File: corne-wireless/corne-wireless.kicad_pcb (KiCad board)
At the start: 2 copper layers, 275.5 x 105.6 mm, 116 parts, among them J2 OLED, J4 OLED, SW1 SW_PUSH, SW10 SW_PUSH, SW11 SW_PUSH, SW12 SW_PUSH, SW13 SW_PUSH, SW14 SW_PUSH, SW15 SW_PUSH, SW16 SW_PUSH, SW17 SW_PUSH, SW18 SW_PUSH, SW19 SW_PUSH, SW2 SW_PUSH, SW20 SW_PUSH, SW21 SW_PUSH, SW22 SW_PUSH, SW23 SW_PUSH, SW24 SW_PUSH, SW25 SW_PUSH, SW26 SW_PUSH, SW27 SW_PUSH, SW28 SW_PUSH, SW29 SW_PUSH, SW3 SW_PUSH, SW30 SW_PUSH, SW31 SW_PUSH, SW32 SW_PUSH, SW33 SW_PUSH, SW34 SW_PUSH, SW35 SW_PUSH, SW36 SW_PUSH, SW37 SW_PUSH, SW38 SW_PUSH, SW39 SW_PUSH, SW4 SW_PUSH, SW40 SW_PUSH, SW41 SW_PUSH, SW42 SW_PUSH, SW5 SW_PUSH, SW6 SW_PUSH, SW7 SW_PUSH, SW8 SW_PUSH, SW9 SW_PUSH, U1 ProMicro, U2 ProMicro

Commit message: Restart
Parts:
- added J1: MJ-4PP-9, kbd:MJ-4PP-9_1side, F.Cu at (144.1, 74.3)
- added J3: MJ-4PP-9, kbd:MJ-4PP-9_1side, F.Cu at (152.5, 74.3)
- added LED1: WS2812B, LED_SMD:LED_WS2812B_PLCC4_5.0x5.0mm_P3.2mm, B.Cu at (39.1, 45.3)
- added LED10: YS-SK6812MINI-E, kbd:YS-SK6812MINI-E, B.Cu at (77.1, 33.4)
- added LED11: YS-SK6812MINI-E, kbd:YS-SK6812MINI-E, B.Cu at (96.1, 35.8)
- added LED12: YS-SK6812MINI-E, kbd:YS-SK6812MINI-E, B.Cu at (115.1, 38.2)
- added LED13: YS-SK6812MINI-E, kbd:YS-SK6812MINI-E, B.Cu at (20.1, 59.5)
- added LED14: YS-SK6812MINI-E, kbd:YS-SK6812MINI-E, B.Cu at (39.1, 59.5)
- added LED15: YS-SK6812MINI-E, kbd:YS-SK6812MINI-E, B.Cu at (58.1, 54.8)
- added LED16: YS-SK6812MINI-E, kbd:YS-SK6812MINI-E, B.Cu at (77.1, 52.4)
- added LED17: YS-SK6812MINI-E, kbd:YS-SK6812MINI-E, B.Cu at (96.1, 54.8)
- added LED18: YS-SK6812MINI-E, kbd:YS-SK6812MINI-E, B.Cu at (115.1, 57.2)
- added LED19: YS-SK6812MINI-E, kbd:YS-SK6812MINI-E, B.Cu at (20.1, 78.5)
- added LED2: WS2812B, LED_SMD:LED_WS2812B_PLCC4_5.0x5.0mm_P3.2mm, B.Cu at (77.1, 38.2)
- added LED20: YS-SK6812MINI-E, kbd:YS-SK6812MINI-E, B.Cu at (39.1, 78.5)
- added LED21: YS-SK6812MINI-E, kbd:YS-SK6812MINI-E, B.Cu at (58.1, 73.8)
- added LED22: YS-SK6812MINI-E, kbd:YS-SK6812MINI-E, B.Cu at (77.1, 71.4)
- added LED23: YS-SK6812MINI-E, kbd:YS-SK6812MINI-E, B.Cu at (96.1, 73.8)
- added LED24: YS-SK6812MINI-E, kbd:YS-SK6812MINI-E, B.Cu at (115.1, 76.2)
- added LED25: YS-SK6812MINI-E, kbd:YS-SK6812MINI-E, B.Cu at (86.6, 93.4)
- added LED26: YS-SK6812MINI-E, kbd:YS-SK6812MINI-E, B.Cu at (106.4, 96.0)
- added LED27: YS-SK6812MINI-E, kbd:YS-SK6812MINI-E, B.Cu at (134.0, 97.5)
- added LED28: WS2812B, LED_SMD:LED_WS2812B_PLCC4_5.0x5.0mm_P3.2mm, B.Cu at (257.6, 45.3)
- added LED29: WS2812B, LED_SMD:LED_WS2812B_PLCC4_5.0x5.0mm_P3.2mm, B.Cu at (219.6, 38.2)
- added LED3: WS2812B, LED_SMD:LED_WS2812B_PLCC4_5.0x5.0mm_P3.2mm, B.Cu at (115.1, 42.9)
- added LED30: WS2812B, LED_SMD:LED_WS2812B_PLCC4_5.0x5.0mm_P3.2mm, B.Cu at (181.6, 42.9)
- added LED31: WS2812B, LED_SMD:LED_WS2812B_PLCC4_5.0x5.0mm_P3.2mm, B.Cu at (257.6, 64.3)
- added LED32: WS2812B, LED_SMD:LED_WS2812B_PLCC4_5.0x5.0mm_P3.2mm, B.Cu at (219.6, 76.2)
- added LED33: WS2812B, LED_SMD:LED_WS2812B_PLCC4_5.0x5.0mm_P3.2mm, B.Cu at (181.6, 80.9)
- added LED34: YS-SK6812MINI-E, kbd:YS-SK6812MINI-E, B.Cu at (276.6, 40.5)
- added LED35: YS-SK6812MINI-E, kbd:YS-SK6812MINI-E, B.Cu at (257.6, 40.5)
- added LED36: YS-SK6812MINI-E, kbd:YS-SK6812MINI-E, B.Cu at (238.6, 35.8)
- added LED37: YS-SK6812MINI-E, kbd:YS-SK6812MINI-E, B.Cu at (219.6, 33.4)
- added LED38: YS-SK6812MINI-E, kbd:YS-SK6812MINI-E, B.Cu at (200.6, 35.8)
- added LED39: YS-SK6812MINI-E, kbd:YS-SK6812MINI-E, B.Cu at (181.6, 38.2)
- added LED4: WS2812B, LED_SMD:LED_WS2812B_PLCC4_5.0x5.0mm_P3.2mm, B.Cu at (39.1, 64.3)
- added LED40: YS-SK6812MINI-E, kbd:YS-SK6812MINI-E, B.Cu at (276.6, 59.5)
- added LED41: YS-SK6812MINI-E, kbd:YS-SK6812MINI-E, B.Cu at (257.6, 59.5)
- added LED42: YS-SK6812MINI-E, kbd:YS-SK6812MINI-E, B.Cu at (238.6, 54.8)
- added LED43: YS-SK6812MINI-E, kbd:YS-SK6812MINI-E, B.Cu at (219.6, 52.4)
- added LED44: YS-SK6812MINI-E, kbd:YS-SK6812MINI-E, B.Cu at (200.6, 54.8)
- added LED45: YS-SK6812MINI-E, kbd:YS-SK6812MINI-E, B.Cu at (181.6, 57.2)
- added LED46: YS-SK6812MINI-E, kbd:YS-SK6812MINI-E, B.Cu at (276.6, 78.5)
- added LED47: YS-SK6812MINI-E, kbd:YS-SK6812MINI-E, B.Cu at (257.6, 78.5)
- added LED48: YS-SK6812MINI-E, kbd:YS-SK6812MINI-E, B.Cu at (238.6, 73.8)
- added LED49: YS-SK6812MINI-E, kbd:YS-SK6812MINI-E, B.Cu at (219.6, 71.4)
- added LED5: WS2812B, LED_SMD:LED_WS2812B_PLCC4_5.0x5.0mm_P3.2mm, B.Cu at (77.1, 76.2)
- added LED50: YS-SK6812MINI-E, kbd:YS-SK6812MINI-E, B.Cu at (200.6, 73.8)
- added LED51: YS-SK6812MINI-E, kbd:YS-SK6812MINI-E, B.Cu at (181.6, 76.2)
- added LED52: YS-SK6812MINI-E, kbd:YS-SK6812MINI-E, B.Cu at (210.1, 93.4)
- added LED53: YS-SK6812MINI-E, kbd:YS-SK6812MINI-E, B.Cu at (190.3, 96.0)
- added LED54: YS-SK6812MINI-E, kbd:YS-SK6812MINI-E, B.Cu at (162.8, 97.5)
- added LED6: WS2812B, LED_SMD:LED_WS2812B_PLCC4_5.0x5.0mm_P3.2mm, B.Cu at (115.1, 80.9)
- added LED7: YS-SK6812MINI-E, kbd:YS-SK6812MINI-E, B.Cu at (20.1, 40.5)
- added LED8: YS-SK6812MINI-E, kbd:YS-SK6812MINI-E, B.Cu at (39.1, 40.5)
- added LED9: YS-SK6812MINI-E, kbd:YS-SK6812MINI-E, B.Cu at (58.1, 35.8)
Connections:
- D1 pad 1: row0 -> unconnected-(D1-K-Pad1)
- D1 pad 2: Net-(D1-Pad2) -> Net-(D1-A)
- D10 pad 1: row1 -> unconnected-(D10-K-Pad1)
- D10 pad 2: Net-(D10-Pad2) -> Net-(D10-A)
- D11 pad 1: row1 -> unconnected-(D11-K-Pad1)
- D11 pad 2: Net-(D11-Pad2) -> Net-(D11-A)
- D12 pad 2: Net-(D12-Pad2) -> Net-(D12-A)
- D13 pad 1: row2 -> unconnected-(D13-K-Pad1)
- D13 pad 2: Net-(D13-Pad2) -> Net-(D13-A)
- D14 pad 1: row2 -> unconnected-(D14-K-Pad1)
- D14 pad 2: Net-(D14-Pad2) -> Net-(D14-A)
- D15 pad 1: row2 -> unconnected-(D15-K-Pad1)
- D15 pad 2: Net-(D15-Pad2) -> Net-(D15-A)
- D16 pad 1: row2 -> unconnected-(D16-K-Pad1)
- D16 pad 2: Net-(D16-Pad2) -> Net-(D16-A)
- D17 pad 1: row2 -> unconnected-(D17-K-Pad1)
- D17 pad 2: Net-(D17-Pad2) -> Net-(D17-A)
- D18 pad 2: Net-(D18-Pad2) -> Net-(D18-A)
- D19 pad 1: row3 -> unconnected-(D19-K-Pad1)
- D19 pad 2: Net-(D19-Pad2) -> Net-(D19-A)
- D2 pad 1: row0 -> unconnected-(D2-K-Pad1)
- D2 pad 2: Net-(D2-Pad2) -> Net-(D2-A)
- D20 pad 1: row3 -> unconnected-(D20-K-Pad1)
- D20 pad 2: Net-(D20-Pad2) -> Net-(D20-A)
- D21 pad 2: Net-(D21-Pad2) -> Net-(D21-A)
- D22 pad 1: row0_r -> unconnected-(D22-K-Pad1)
- D22 pad 2: Net-(D22-Pad2) -> Net-(D22-A)
- D23 pad 1: row0_r -> unconnected-(D23-K-Pad1)
- D23 pad 2: Net-(D23-Pad2) -> Net-(D23-A)
- D24 pad 1: row0_r -> unconnected-(D24-K-Pad1)
- D24 pad 2: Net-(D24-Pad2) -> Net-(D24-A)
- D25 pad 1: row0_r -> unconnected-(D25-K-Pad1)
- D25 pad 2: Net-(D25-Pad2) -> Net-(D25-A)
- D26 pad 1: row0_r -> unconnected-(D26-K-Pad1)
- D26 pad 2: Net-(D26-Pad2) -> Net-(D26-A)
- D27 pad 2: Net-(D27-Pad2) -> Net-(D27-A)
- D28 pad 1: row1_r -> unconnected-(D28-K-Pad1)
- D28 pad 2: Net-(D28-Pad2) -> Net-(D28-A)
- D29 pad 1: row1_r -> unconnected-(D29-K-Pad1)
- D29 pad 2: Net-(D29-Pad2) -> Net-(D29-A)
- D3 pad 1: row0 -> unconnected-(D3-K-Pad1)
- D3 pad 2: Net-(D3-Pad2) -> Net-(D3-A)
- D30 pad 1: row1_r -> unconnected-(D30-K-Pad1)
- D30 pad 2: Net-(D30-Pad2) -> Net-(D30-A)
- D31 pad 1: row1_r -> unconnected-(D31-K-Pad1)
- D31 pad 2: Net-(D31-Pad2) -> Net-(D31-A)
- D32 pad 1: row1_r -> unconnected-(D32-K-Pad1)
- D32 pad 2: Net-(D32-Pad2) -> Net-(D32-A)
- D33 pad 2: Net-(D33-Pad2) -> Net-(D33-A)
- D34 pad 1: row2_r -> unconnected-(D34-K-Pad1)
- D34 pad 2: Net-(D34-Pad2) -> Net-(D34-A)
- D35 pad 1: row2_r -> unconnected-(D35-K-Pad1)
- D35 pad 2: Net-(D35-Pad2) -> Net-(D35-A)
- D36 pad 1: row2_r -> unconnected-(D36-K-Pad1)
- D36 pad 2: Net-(D36-Pad2) -> Net-(D36-A)
- D37 pad 1: row2_r -> unconnected-(D37-K-Pad1)
- D37 pad 2: Net-(D37-Pad2) -> Net-(D37-A)
- D38 pad 1: row2_r -> unconnected-(D38-K-Pad1)
- D38 pad 2: Net-(D38-Pad2) -> Net-(D38-A)
- D39 pad 2: Net-(D39-Pad2) -> Net-(D39-A)
- D4 pad 1: row0 -> unconnected-(D4-K-Pad1)
- D4 pad 2: Net-(D4-Pad2) -> Net-(D4-A)
- D40 pad 1: row3_r -> unconnected-(D40-K-Pad1)
- D40 pad 2: Net-(D40-Pad2) -> Net-(D40-A)
- D41 pad 1: row3_r -> unconnected-(D41-K-Pad1)
- D41 pad 2: Net-(D41-Pad2) -> Net-(D41-A)
- D42 pad 2: Net-(D42-Pad2) -> Net-(D42-A)
- D5 pad 1: row0 -> unconnected-(D5-K-Pad1)
- D5 pad 2: Net-(D5-Pad2) -> Net-(D5-A)
- D6 pad 2: Net-(D6-Pad2) -> Net-(D6-A)
- D7 pad 1: row1 -> unconnected-(D7-K-Pad1)
- D7 pad 2: Net-(D7-Pad2) -> Net-(D7-A)
- D8 pad 1: row1 -> unconnected-(D8-K-Pad1)
- D8 pad 2: Net-(D8-Pad2) -> Net-(D8-A)
- D9 pad 1: row1 -> unconnected-(D9-K-Pad1)
- D9 pad 2: Net-(D9-Pad2) -> Net-(D9-A)
- SW1 pad 2: unconnected-(SW1-Pad2) -> Net-(D1-A)
- SW10 pad 2: unconnected-(SW10-Pad2) -> Net-(D10-A)
- SW11 pad 2: unconnected-(SW11-Pad2) -> Net-(D11-A)
- SW12 pad 2: unconnected-(SW12-Pad2) -> Net-(D12-A)
- SW13 pad 2: unconnected-(SW13-Pad2) -> Net-(D13-A)
- SW14 pad 2: unconnected-(SW14-Pad2) -> Net-(D14-A)
- SW15 pad 2: unconnected-(SW15-Pad2) -> Net-(D15-A)
- SW16 pad 2: unconnected-(SW16-Pad2) -> Net-(D16-A)
- SW17 pad 2: unconnected-(SW17-Pad2) -> Net-(D17-A)
- SW18 pad 2: unconnected-(SW18-Pad2) -> Net-(D18-A)
- SW19 pad 2: unconnected-(SW19-Pad2) -> Net-(D19-A)
- SW2 pad 2: unconnected-(SW2-Pad2) -> Net-(D2-A)
- SW20 pad 2: unconnected-(SW20-Pad2) -> Net-(D20-A)
- SW21 pad 2: unconnected-(SW21-Pad2) -> Net-(D21-A)
- SW22 pad 2: unconnected-(SW22-Pad2) -> Net-(D22-A)
- SW23 pad 2: unconnected-(SW23-Pad2) -> Net-(D23-A)
- SW24 pad 2: unconnected-(SW24-Pad2) -> Net-(D24-A)
- SW25 pad 2: unconnected-(SW25-Pad2) -> Net-(D25-A)
- SW26 pad 2: unconnected-(SW26-Pad2) -> Net-(D26-A)
- SW27 pad 2: unconnected-(SW27-Pad2) -> Net-(D27-A)
- SW28 pad 2: unconnected-(SW28-Pad2) -> Net-(D28-A)
- SW29 pad 2: unconnected-(SW29-Pad2) -> Net-(D29-A)
- SW3 pad 2: unconnected-(SW3-Pad2) -> Net-(D3-A)
- SW30 pad 2: unconnected-(SW30-Pad2) -> Net-(D30-A)
- SW31 pad 2: unconnected-(SW31-Pad2) -> Net-(D31-A)
- SW32 pad 2: unconnected-(SW32-Pad2) -> Net-(D32-A)
- SW33 pad 2: unconnected-(SW33-Pad2) -> Net-(D33-A)
- SW34 pad 2: unconnected-(SW34-Pad2) -> Net-(D34-A)
- SW35 pad 2: unconnected-(SW35-Pad2) -> Net-(D35-A)
- SW36 pad 2: unconnected-(SW36-Pad2) -> Net-(D36-A)
- SW37 pad 2: unconnected-(SW37-Pad2) -> Net-(D37-A)
- SW38 pad 2: unconnected-(SW38-Pad2) -> Net-(D38-A)
- SW39 pad 2: unconnected-(SW39-Pad2) -> Net-(D39-A)
- SW4 pad 2: unconnected-(SW4-Pad2) -> Net-(D4-A)
- SW40 pad 2: unconnected-(SW40-Pad2) -> Net-(D40-A)
- SW41 pad 2: unconnected-(SW41-Pad2) -> Net-(D41-A)
- SW42 pad 2: unconnected-(SW42-Pad2) -> Net-(D42-A)
- SW5 pad 2: unconnected-(SW5-Pad2) -> Net-(D5-A)
- SW6 pad 2: unconnected-(SW6-Pad2) -> Net-(D6-A)
- SW7 pad 2: unconnected-(SW7-Pad2) -> Net-(D7-A)
- SW8 pad 2: unconnected-(SW8-Pad2) -> Net-(D8-A)
- SW9 pad 2: unconnected-(SW9-Pad2) -> Net-(D9-A)
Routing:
- net GND: track 49.9 -> 637.2 mm, vias 0 -> 16
- net GNDA: track 49.6 -> 617.9 mm, vias 0 -> 15
- net VDD: track 37.6 -> 573.1 mm, vias 0 -> 2
- net VCC: track 37.3 -> 544.3 mm, vias 0 -> 2
- net data: track 0.00 -> 77.0 mm
- net Net-(LED31-Pad2): track 0.00 -> 71.8 mm, vias 0 -> 2
- net data_r: track 0.00 -> 62.9 mm
- net Net-(LED1-Pad4): track 0.00 -> 47.8 mm
- net Net-(LED32-Pad2): track 0.00 -> 47.4 mm
- net Net-(LED2-Pad4): track 0.00 -> 46.3 mm
- net Net-(LED4-Pad2): track 0.00 -> 43.6 mm, vias 0 -> 2
- net Net-(LED28-Pad2): track 0.00 -> 41.5 mm, vias 0 -> 2
- net LED: track 0.00 -> 41.1 mm
- net Net-(D21-Pad2): track 38.3 -> 0.00 mm
- net Net-(D21-A): track 0.00 -> 38.3 mm
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
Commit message: Prep for removal of OLED headers
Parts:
- removed J1, J3: MJ-4PP-9, kbd:MJ-4PP-9_1side
- removed J2, J4: OLED, kbd:OLED_1side
- removed LED1, LED2, LED28, LED29, LED3, LED30, LED31, LED32, LED33, LED4, LED5, LED6: WS2812B, LED_SMD:LED_WS2812B_PLCC4_5.0x5.0mm_P3.2mm
- removed LED10, LED11, LED12, LED13, LED14, LED15, LED16, LED17, LED18, LED19, LED20, LED21, LED22, LED23, LED24, LED25, LED26, LED27, LED34, LED35, LED36, LED37, LED38, LED39, LED40, LED41, LED42, LED43, LED44, LED45, LED46, LED47, LED48, LED49, LED50, LED51, LED52, LED53, LED54, LED7, LED8, LED9: YS-SK6812MINI-E, kbd:YS-SK6812MINI-E
- added OL1: OLED, kbd:OLED_1side, F.Cu at (130.9, 67.2)
- added OL2: OLED, kbd:OLED_1side, F.Cu at (158.3, 67.2)
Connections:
- D1 pad 1: unconnected-(D1-K-Pad1) -> row0
- D10 pad 1: unconnected-(D10-K-Pad1) -> row1
- D11 pad 1: unconnected-(D11-K-Pad1) -> row1
- D13 pad 1: unconnected-(D13-K-Pad1) -> row2
- D14 pad 1: unconnected-(D14-K-Pad1) -> row2
- D15 pad 1: unconnected-(D15-K-Pad1) -> row2
- D16 pad 1: unconnected-(D16-K-Pad1) -> row2
- D17 pad 1: unconnected-(D17-K-Pad1) -> row2
- D19 pad 1: unconnected-(D19-K-Pad1) -> row3
- D2 pad 1: unconnected-(D2-K-Pad1) -> row0
- D20 pad 1: unconnected-(D20-K-Pad1) -> row3
- D22 pad 1: unconnected-(D22-K-Pad1) -> row0_r
- D23 pad 1: unconnected-(D23-K-Pad1) -> row0_r
- D24 pad 1: unconnected-(D24-K-Pad1) -> row0_r
- D25 pad 1: unconnected-(D25-K-Pad1) -> row0_r
- D26 pad 1: unconnected-(D26-K-Pad1) -> row0_r
- D28 pad 1: unconnected-(D28-K-Pad1) -> row1_r
- D29 pad 1: unconnected-(D29-K-Pad1) -> row1_r
- D3 pad 1: unconnected-(D3-K-Pad1) -> row0
- D30 pad 1: unconnected-(D30-K-Pad1) -> row1_r
- D31 pad 1: unconnected-(D31-K-Pad1) -> row1_r
- D32 pad 1: unconnected-(D32-K-Pad1) -> row1_r
- D34 pad 1: unconnected-(D34-K-Pad1) -> row2_r
- D35 pad 1: unconnected-(D35-K-Pad1) -> row2_r
- D36 pad 1: unconnected-(D36-K-Pad1) -> row2_r
- D37 pad 1: unconnected-(D37-K-Pad1) -> row2_r
- D38 pad 1: unconnected-(D38-K-Pad1) -> row2_r
- D4 pad 1: unconnected-(D4-K-Pad1) -> row0
- D40 pad 1: unconnected-(D40-K-Pad1) -> row3_r
- D41 pad 1: unconnected-(D41-K-Pad1) -> row3_r
- D5 pad 1: unconnected-(D5-K-Pad1) -> row0
- D7 pad 1: unconnected-(D7-K-Pad1) -> row1
- D8 pad 1: unconnected-(D8-K-Pad1) -> row1
- D9 pad 1: unconnected-(D9-K-Pad1) -> row1
- RSW1 pad 2: unconnected-(RSW1-Pad2) -> GND1
- RSW2 pad 2: unconnected-(RSW2-Pad2) -> GND2
- U1 pad 21: unconnected-(U1-VCC-Pad21) -> VCC
- U1 pad 23: unconnected-(U1-GND-Pad23) -> GND1
- U1 pad 3: Net-(U1-GND-Pad3) -> GND1
- U1 pad 4: Net-(U1-GND-Pad3) -> GND1
- U2 pad 21: unconnected-(U2-VCC-Pad21) -> VDD
- U2 pad 23: unconnected-(U2-GND-Pad23) -> GND2
- U2 pad 3: Net-(U2-GND-Pad3) -> GND2
- U2 pad 4: Net-(U2-GND-Pad3) -> GND2
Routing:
- net GND: track 637.2 -> 0.00 mm, vias 16 -> 0
- net GNDA: track 617.9 -> 0.00 mm, vias 15 -> 0
- net VDD: track 573.1 -> 37.6 mm, vias 2 -> 0
- net VCC: track 544.3 -> 37.3 mm, vias 2 -> 0
- net GND2: track 0.00 -> 78.1 mm
- net data: track 77.0 -> 0.00 mm
- net Net-(LED31-Pad2): track 71.8 -> 0.00 mm, vias 2 -> 0
- net data_r: track 62.9 -> 0.00 mm
- net GND1: track 0.00 -> 49.9 mm
- net Net-(LED1-Pad4): track 47.8 -> 0.00 mm
- net Net-(LED32-Pad2): track 47.4 -> 0.00 mm
- net Net-(LED2-Pad4): track 46.3 -> 0.00 mm
- net Net-(LED4-Pad2): track 43.6 -> 0.00 mm, vias 2 -> 0
- net Net-(LED28-Pad2): track 41.5 -> 0.00 mm, vias 2 -> 0
- net LED: track 41.1 -> 0.00 mm
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
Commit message: Finalize PCB
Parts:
- removed OL1, OL2: OLED, kbd:OLED_1side
- added J1: Conn_01x02, Connector_JST:JST_SH_BM02B-SRSS-TB_1x02-1MP_P1.00mm_Vertical, F.Cu at (129.7, 67.4)
- added J2: Conn_01x02, Connector_JST:JST_SH_BM02B-SRSS-TB_1x02-1MP_P1.00mm_Vertical, F.Cu at (167.2, 67.4)
- added PMOS1: SSM3J328R, corne-wireless-fp:SOT-23F, F.Cu at (133.6, 74.2)
- added PMOS2: SSM3J328R, corne-wireless-fp:SOT-23F, F.Cu at (163.6, 74.2)
- added SW1: SW_SPDT, Button_Switch_SMD:SW_SPDT_PCM12, F.Cu at (142.8, 76.3)
- added SW23: SW_SPDT, Button_Switch_SMD:SW_SPDT_PCM12, F.Cu at (154.4, 76.3)
- renumbered D4 to D10, D10 to D11, D16 to D12, D19 to D13, D5 to D14, D11 to D15, D17 to D16, D20 to D17, D6 to D18, D12 to D19, D7 to D2, D18 to D20, D28 to D23, D34 to D24, D23 to D25, D29 to D26, D35 to D27, D24 to D28, D30 to D29, D13 to D3, D36 to D30, D25 to D31, D31 to D32, D37 to D33, D40 to D34, D26 to D35, D32 to D36, D38 to D37, D41 to D38, D27 to D39, D2 to D4, D33 to D40, D39 to D41, D8 to D5, D14 to D6, D3 to D7, D9 to D8, D15 to D9, SW15 to SW10, SW4 to SW11, SW10 to SW12, SW16 to SW13, SW19 to SW14, SW5 to SW15, SW11 to SW16, SW20 to SW18, SW6 to SW19, SW1 to SW2, SW12 to SW20, SW18 to SW21, SW21 to SW22, SW22 to SW24, SW28 to SW25, SW34 to SW26, SW23 to SW27, SW29 to SW28, SW35 to SW29, SW7 to SW3, SW24 to SW30, SW30 to SW31, SW36 to SW32, SW25 to SW33, SW31 to SW34, SW37 to SW35, SW40 to SW36, SW26 to SW37, SW32 to SW38, SW38 to SW39, SW13 to SW4, SW41 to SW40, SW27 to SW41, SW33 to SW42, SW39 to SW43, SW42 to SW44, SW2 to SW5, SW8 to SW6, SW14 to SW7, SW3 to SW8
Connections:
- U1 pad 1: LED -> unconnected-(U1-TX0/D3-Pad1)
- U1 pad 2: data -> unconnected-(U1-RX1/D2-Pad2)
- U1 pad 24: unconnected-(U1-RAW-Pad24) -> battery+
- U2 pad 1: LED_r -> unconnected-(U2-TX0/D3-Pad1)
- U2 pad 2: data_r -> unconnected-(U2-RX1/D2-Pad2)
- U2 pad 24: unconnected-(U2-RAW-Pad24) -> battery+_r
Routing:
- net battery+: track 0.00 -> 53.7 mm
- net battery+_r: track 0.00 -> 49.9 mm
- net reset_r: track 85.4 -> 40.0 mm
- net VDD: track 37.6 -> 0.00 mm
- net VCC: track 37.3 -> 0.00 mm
- net SDA_r: track 32.7 -> 0.00 mm
- net SDA: track 32.4 -> 0.00 mm
- net SCL_r: track 27.9 -> 0.00 mm
- net SCL: track 27.7 -> 0.00 mm
- net GND1: track 49.9 -> 70.1 mm, vias 0 -> 3
- net reset: track 60.0 -> 45.8 mm, vias 0 -> 2
- net Net-(J1-Pin_1): track 0.00 -> 7.87 mm
- net Net-(PMOS1-S): track 0.00 -> 7.39 mm
- net Net-(PMOS2-S): track 0.00 -> 7.19 mm
- net Net-(J2-Pin_1): track 0.00 -> 6.89 mm
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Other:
- rule pad_to_mask_clearance: 0.2 -> 0

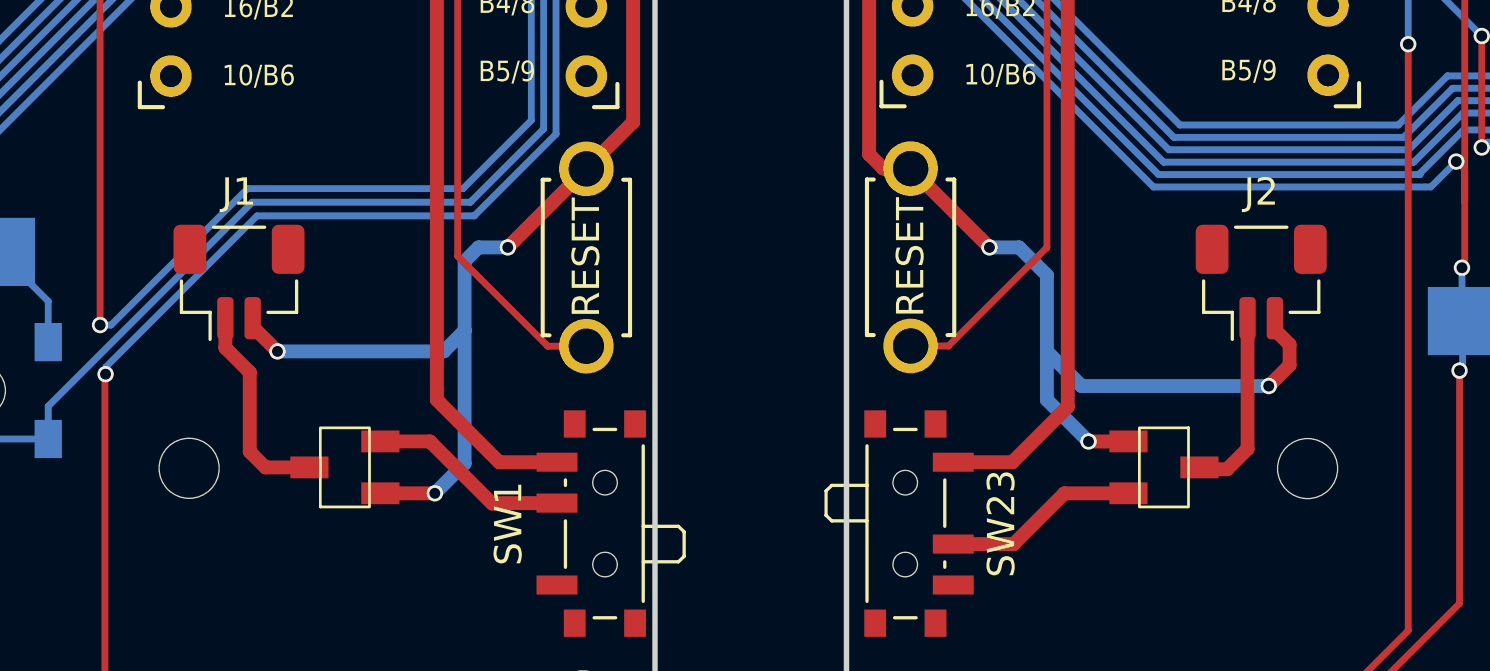
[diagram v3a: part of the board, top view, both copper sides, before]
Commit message: Change JST SH connector to PH
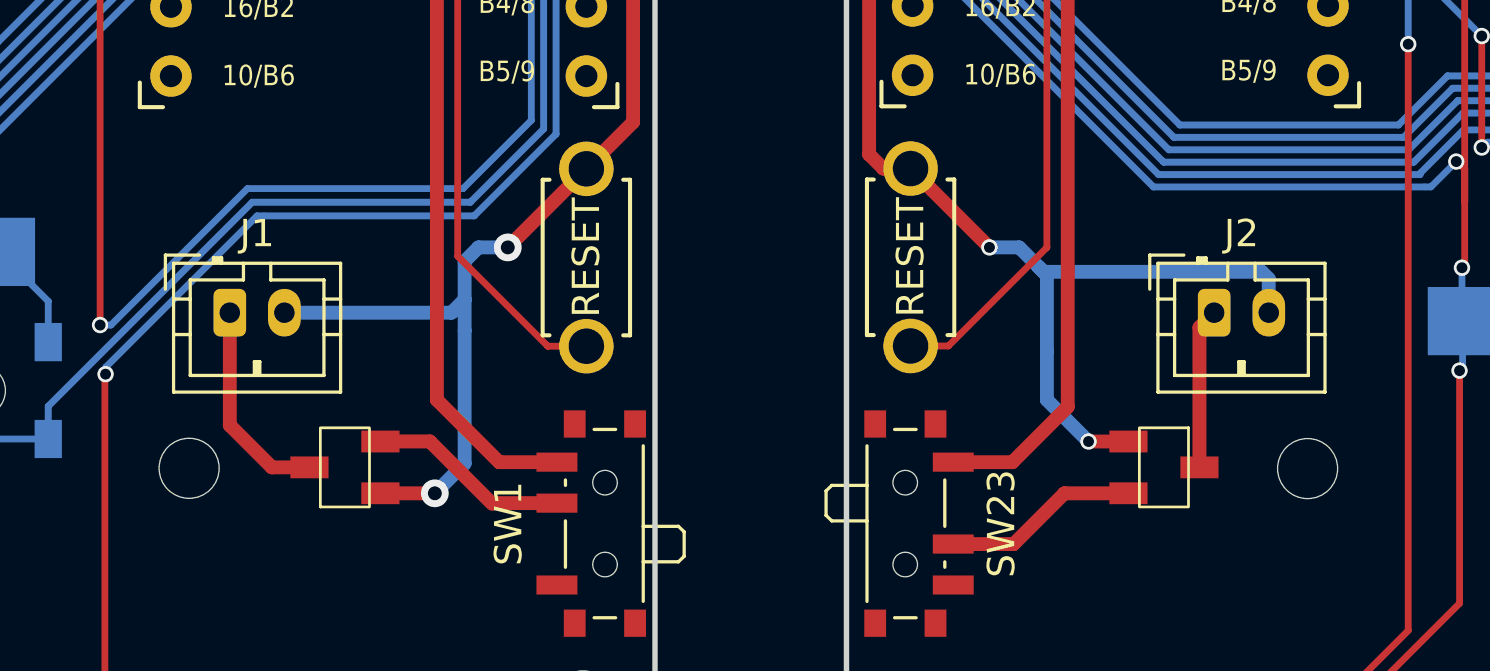
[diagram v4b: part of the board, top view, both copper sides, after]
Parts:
- J1, J2: footprint Connector_JST:JST_SH_BM02B-SRSS-TB_1x02-1MP_P1.00mm_Vertical -> Connector_JST:JST_PH_B2B-PH-K_1x02_P2.00mm_Vertical
- moved J2 2.06 mm to (165.4, 68.6)
- moved J1 1.17 mm to (129.4, 68.6)
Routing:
- net GND1: track 70.1 -> 67.6 mm, vias 3 -> 2
- net GND2: track 76.1 -> 74.3 mm, vias 3 -> 2
- net Net-(J2-Pin_1): track 6.89 -> 5.94 mm

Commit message: Finalize PCB
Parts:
- moved SW23 0.24 mm to (154.2, 76.3)
- moved SW1 0.15 mm to (142.6, 76.3)
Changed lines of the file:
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@@
     (tags "mounting hole 2.2mm no annular m2")
     (attr exclude_from_pos_files exclude_from_bom)
-    (fp_text reference "Ref**" (at -0.95 -0.55) (layer "F.Fab") hide
+    (fp_text reference "Ref**" (at 0.188 2.708) (layer "F.Fab") hide
         (effects (font (size 1 1) (thickness 0.15)))
     )
-    (fp_text value "Val**" (at 0 0.55) (layer "F.Fab") hide
+    (fp_text value "Val**" (at -0.066 0.93) (layer "F.Fab") hide
         (effects (font (size 1 1) (thickness 0.15)))
     )
@@
         (effects (font (size 1 1) (thickness 0.15)))
     )
-    (fp_text value "Conn_01x02" (at 1 4) (layer "F.Fab") hide
+    (fp_text value "Conn_01x02" (at 0.73 4.092) (layer "F.Fab") hide
         (effects (font (size 1 1) (thickness 0.15)))
     )
@@
   )
   (footprint "Button_Switch_SMD:SW_SPDT_PCM12" (layer "F.Cu")
-    (at 142.7775 76.28 90)
+    (at 142.6295 76.28 90)
     (descr "Ultraminiature Surface Mount Slide Switch, right-angle, https://www.ckswitches.com/media/1424/pcm.pdf")
     (property "Sheetfile" "corne-wireless.kicad_sch")
@@
   )
   (footprint "Button_Switch_SMD:SW_SPDT_PCM12" (layer "F.Cu")
-    (at 154.4375 76.28 -90)
+    (at 154.2015 76.28 -90)
     (descr "Ultraminiature Surface Mount Slide Switch, right-angle, https://www.ckswitches.com/media/1424/pcm.pdf")
     (property "Sheetfile" "corne-wireless.kicad_sch")
@@
   (segment (start 153.621901 35.214999) (end 153.414501 35.214999) (width 0.508) (layer "F.Cu") (net 11))
   (segment (start 152.7845 62.752) (end 153.3045 63.272) (width 0.508) (layer "F.Cu") (net 11))
-  (segment (start 162.2855 73.272) (end 162.2875 73.27) (width 0.508) (layer "F.Cu") (net 11))
+  (segment (start 162.240616 73.316884) (end 162.2875 73.27) (width 0.508) (layer "F.Cu") (net 11))
+  (segment (start 160.106384 73.316884) (end 162.240616 73.316884) (width 0.508) (layer "F.Cu") (net 11))
   (segment (start 154.3045 63.272) (end 157.1925 66.16) (width 0.508) (layer "F.Cu") (net 11))
-  (segment (start 160.8235 73.272) (end 162.2855 73.272) (width 0.508) (layer "F.Cu") (net 11))
-  (via (at 157.1925 66.16) (size 0.6) (drill 0.4) (layers "F.Cu" "B.Cu") (net 11))
-  (via (at 160.8235 73.272) (size 0.6) (drill 0.4) (layers "F.Cu" "B.Cu") (net 11))
+  (via (at 157.1925 66.16) (size 1.016) (drill 0.508) (layers "F.Cu" "B.Cu") (net 11))
+  (via (at 160.106384 73.316884) (size 1.016) (drill 0.508) (layers "F.Cu" "B.Cu") (net 11))
   (segment (start 154.3839 34.453) (end 167.0639 34.453) (width 0.508) (layer "B.Cu") (net 11))
   (segment (start 167.0639 34.453) (end 169.6039 36.993) (width 0.508) (layer "B.Cu") (net 11))
   (segment (start 159.1795 67.056) (end 158.9855 66.862) (width 0.508) (layer "B.Cu") (net 11))
-  (segment (start 159.2995 71.748) (end 160.8235 73.272) (width 0.508) (layer "B.Cu") (net 11))
-  (segment (start 158.9855 66.862) (end 159.2995 67.176) (width 0.508) (layer "B.Cu") (net 11))
+  (segment (start 159.2995 72.51) (end 159.2995 67.176) (width 0.508) (layer "B.Cu") (net 11))
+  (segment (start 159.2995 67.176) (end 158.9855 66.862) (width 0.508) (layer "B.Cu") (net 11))
   (segment (start 167.4275 68.552) (end 167.4275 67.31) (width 0.508) (layer "B.Cu") (net 11))
-  (segment (start 159.2995 69.97) (end 159.2995 71.748) (width 0.508) (layer "B.Cu") (net 11))
   (segment (start 157.1925 66.16) (end 158.2835 66.16) (width 0.508) (layer "B.Cu") (net 11))
-  (segment (start 159.2995 67.176) (end 159.2995 69.97) (width 0.508) (layer "B.Cu") (net 11))
+  (segment (start 160.106384 73.316884) (end 159.2995 72.51) (width 0.508) (layer "B.Cu") (net 11))
   (segment (start 167.4275 67.31) (end 167.1735 67.056) (width 0.508) (layer "B.Cu") (net 11))
   (segment (start 167.1735 67.056) (end 159.1795 67.056) (width 0.508) (layer "B.Cu") (net 11))
@@
   (segment (start 263.4565 30.695) (end 263.4565 30.732) (width 0.25) (layer "B.Cu") (net 46))
   (segment (start 263.4565 30.732) (end 265.2145 32.49) (width 0.25) (layer "B.Cu") (net 46))
+  (segment (start 139.0075 75.53) (end 141.1995 75.53) (width 0.508) (layer "F.Cu") (net 47))
   (segment (start 136.6915 73.27) (end 138.9795 75.558) (width 0.508) (layer "F.Cu") (net 47))
-  (segment (start 139.0075 75.53) (end 141.3475 75.53) (width 0.508) (layer "F.Cu") (net 47))
+  (segment (start 138.9795 75.558) (end 139.0075 75.53) (width 0.508) (layer "F.Cu") (net 47))
   (segment (start 134.8775 73.27) (end 136.6915 73.27) (width 0.508) (layer "F.Cu") (net 47))
   (segment (start 158.0815 77.03) (end 159.9415 75.17) (width 0.508) (layer "F.Cu") (net 50))
-  (segment (start 155.8675 77.03) (end 158.0815 77.03) (width 0.508) (layer "F.Cu") (net 50))
+  (segment (start 158.0815 77.03) (end 155.6315 77.03) (width 0.508) (layer "F.Cu") (net 50))
   (segment (start 159.9415 75.17) (end 162.2875 75.17) (width 0.508) (layer "F.Cu") (net 50))
   (segment (start 154.3045 69.772) (end 155.6875 69.772) (width 0.25) (layer "F.Cu") (net 51))
@@
   (segment (start 139.2295 74.03) (end 136.9475 71.748) (width 0.508) (layer "F.Cu") (net 80))
   (segment (start 136.9475 33.902) (end 134.9875 31.942) (width 0.508) (layer "F.Cu") (net 80))
-  (segment (start 141.3475 74.03) (end 139.2375 74.03) (width 0.508) (layer "F.Cu") (net 80))
+  (segment (start 139.2295 74.03) (end 141.1995 74.03) (width 0.508) (layer "F.Cu") (net 80))
   (segment (start 142.4239 37.022) (end 142.4239 39.562) (width 0.508) (layer "F.Cu") (net 86))
   (segment (start 134.8775 75.17) (end 136.8725 75.17) (width 0.508) (layer "F.Cu") (net 86))
@@
   (segment (start 137.9635 66.668) (end 137.9635 68.072) (width 0.508) (layer "B.Cu") (net 86))
   (segment (start 131.3595 68.552) (end 137.4835 68.552) (width 0.508) (layer "B.Cu") (net 86))
-  (segment (start 158.0335 74.03) (end 155.8675 74.03) (width 0.508) (layer "F.Cu") (net 87))
   (segment (start 158.5795 31.912) (end 160.0615 33.394) (width 0.508) (layer "F.Cu") (net 87))
+  (segment (start 158.0335 74.03) (end 155.6315 74.03) (width 0.508) (layer "F.Cu") (net 87))
   (segment (start 160.0615 33.394) (end 160.0615 72.002) (width 0.508) (layer "F.Cu") (net 87))
   (segment (start 160.0615 72.002) (end 158.0335 74.03) (width 0.508) (layer "F.Cu") (net 87))
